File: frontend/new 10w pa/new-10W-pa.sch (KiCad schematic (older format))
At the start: 44 parts, among them K1 D3002, P1 CONN_01X02, P2 CONN_02X01, P3 From HL CN3, P4 CONN_01X02, P5 CONN_01X02, P6 CONN_01X01, P7 From FE CN2, Q1 2N3906, Q2 2N3906, Q3 RD16HHF1, T1 TRANSFO, T2 TRANSFO, U1 74HC14, U2 74HC14

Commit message: Minor updates to v1.12
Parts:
- removed R9: Microstrip, Resistors_SMD:R_0805, symbol R
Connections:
- wire segments 75 -> 79
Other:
- note added: "Microstrip\nW=15Mil, L=1800Mil"
- note added: "T37-6 8T #26"
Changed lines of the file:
@@
 encoding utf-8
 Sheet 1 3
-Title "Hermes-Lite Basic 10W Power Amplifier with Filters"
-Date "Thursday, January 01, 2015"
-Rev "1.11"
+Title "Hermes-Lite Basic 5W Power Amplifier with Filters"
+Date "Friday, January 02, 2015"
+Rev "1.12"
 Comp "SofterHardware"
 Comment1 "AC9HY"
@@
 Connection ~ 8050 3850
 Connection ~ 5650 4200
-$Comp
-L R R9
-U 1 1 54A5A54D
-P 7200 4450
-F 0 "R9" V 7280 4450 40  0000 C CNN
-F 1 "Microstrip" V 7207 4451 40  0000 C CNN
-F 2 "Resistors_SMD:R_0805" V 7130 4450 30  0001 C CNN
-F 3 "" H 7200 4450 30  0000 C CNN
-	1    7200 4450
-	0    1    1    0
-$EndComp
 Wire Wire Line
 	8050 4250 8050 4600
@@
 Wire Wire Line
 	8850 4250 9100 4250
+Text Notes 9350 4050 0    50   ~ 0
+T37-6 8T #26
+Wire Wire Line
+	6950 4450 6950 5000
+Wire Wire Line
+	6950 5000 7150 5000
+Wire Wire Line
+	7150 5000 7150 4450
+Wire Wire Line
+	7150 4450 7450 4450
+Text Notes 6550 5100 0    50   ~ 0
+Microstrip\nW=15Mil, L=1800Mil
 $EndSCHEMATC

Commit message: Starting Layout
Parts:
- R2, R3, R4: footprint Resistors_SMD:R_0805 -> Resistors_ThroughHole:Resistor_Vertical_RM5mm
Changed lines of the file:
@@
 F 0 "R3" V 5180 4050 40  0000 C CNN
 F 1 "0" V 5107 4051 40  0000 C CNN
-F 2 "Resistors_SMD:R_0805" V 5030 4050 30  0001 C CNN
+F 2 "Resistors_ThroughHole:Resistor_Vertical_RM5mm" V 5030 4050 30  0001 C CNN
 F 3 "" H 5100 4050 30  0000 C CNN
 	1    5100 4050
@@
 F 0 "R2" V 4930 4300 40  0000 C CNN
 F 1 "DNI" V 4857 4301 40  0000 C CNN
-F 2 "Resistors_SMD:R_0805" V 4780 4300 30  0001 C CNN
+F 2 "Resistors_ThroughHole:Resistor_Vertical_RM5mm" V 4780 4300 30  0001 C CNN
 F 3 "" H 4850 4300 30  0000 C CNN
 	1    4850 4300
@@
 F 0 "R4" V 5430 4300 40  0000 C CNN
 F 1 "DNI" V 5357 4301 40  0000 C CNN
-F 2 "Resistors_SMD:R_0805" V 5280 4300 30  0001 C CNN
+F 2 "Resistors_ThroughHole:Resistor_Vertical_RM5mm" V 5280 4300 30  0001 C CNN
 F 3 "" H 5350 4300 30  0000 C CNN
 	1    5350 4300

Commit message: Continuing board routing
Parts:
- removed D1: 1N5231, Diodes_SMD:Diode-SMA_Standard, symbol ZENER
- removed Q2: 2N3906, Transistors_SMD:sot23, symbol PNP
- removed R2, R4: DNI, Resistors_ThroughHole:Resistor_Vertical_RM5mm, symbol R
- removed R3: 0, Resistors_ThroughHole:Resistor_Vertical_RM5mm, symbol R
- removed R8: 220, Resistors_SMD:R_0805, symbol R
- removed T2: TRANSFO, Socket_Strips:Socket_Strip_Straight_2x02, symbol TRANSFO
- added T2: OUT_TRANSF, HERMESLITE:OUT_TRANSF, symbol OUT_TRANSFO
- added U7: LP2951-50D, Housings_SOIC:SOIC-8_3.9x4.9mm_Pitch1.27mm, symbol LP2951-50D
- C1, C11, C12, C13, C14, C3, C4, C5, C6, C7, C8, C9: footprint Capacitors_SMD:C_0805 -> HERMESLITE:C_0805
- K1: footprint Sockets_DIP:DIP-10__300 -> HERMESLITE:D3002
- R1, R10, R5, R6: footprint Resistors_SMD:R_0805 -> HERMESLITE:R_0805
- R7: value 1k -> 10k; footprint Resistors_SMD:R_0805 -> HERMESLITE:R_0805
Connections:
- net labels removed: +PTT
- wire segments 79 -> 93
- no-connect marks 13 -> 14
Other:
- moved on the sheet: C5, P6, R7

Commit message: new superband design and updated pcb
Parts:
- C10: footprint Discret:C1V8 -> Capacitors_Tantalum_SMD:TantalC_SizeB_EIA-3528_Reflow
- C2: footprint Discret:C1V8 -> Capacitors_Tantalum_SMD:TantalC_SizeD_EIA-7343_Reflow
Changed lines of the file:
@@
 F 0 "C2" H 5300 1700 50  0000 L CNN
 F 1 "47uF 16V" H 5400 1600 50  0000 L CNN
-F 2 "Discret:C1V8" H 5250 1600 60  0001 C CNN
+F 2 "Capacitors_Tantalum_SMD:TantalC_SizeD_EIA-7343_Reflow" H 5250 1600 60  0001 C CNN
 F 3 "" H 5250 1600 60  0000 C CNN
 	1    5250 1600
@@
 F 0 "C10" H 8300 3100 50  0000 L CNN
 F 1 "10uF 16V" V 8350 2500 50  0000 L CNN
-F 2 "Discret:C1V8" H 8250 3000 60  0001 C CNN
+F 2 "Capacitors_Tantalum_SMD:TantalC_SizeB_EIA-3528_Reflow" H 8250 3000 60  0001 C CNN
 F 3 "" H 8250 3000 60  0000 C CNN
 	1    8250 3000

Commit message: More pcb changes
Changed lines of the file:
@@
 	3400 1800 3400 1700
 Wire Wire Line
-	3400 1700 4700 1700
+	2500 1700 4700 1700
 Wire Wire Line
 	4700 1000 4700 3400
@@
 Connection ~ 8850 4250
 Connection ~ 8850 3850
+Wire Wire Line
+	3400 2000 3400 2050
+Wire Wire Line
+	2500 2050 4900 2050
+Wire Wire Line
+	4900 2050 4900 2150
+$Comp
+L GND #PWR023
+U 1 1 54BBCE74
+P 4900 2150
+F 0 "#PWR023" H 4900 2150 30  0001 C CNN
+F 1 "GND" H 4900 2080 30  0001 C CNN
+F 2 "" H 4900 2150 60  0000 C CNN
+F 3 "" H 4900 2150 60  0000 C CNN
+	1    4900 2150
+	1    0    0    -1
+$EndComp
+Connection ~ 4900 2150
+Wire Wire Line
+	2500 2000 2500 2050
+Connection ~ 3400 2050
+Wire Wire Line
+	2500 1800 2500 1700
+Connection ~ 3400 1700
+Connection ~ 6000 2100
+Connection ~ 5700 2100
+Connection ~ 4400 800
 $EndSCHEMATC

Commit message: BCD Filter update
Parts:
- removed P3: From HL CN3, Pin_Headers:Pin_Header_Straight_2x06, symbol CONN_02X06
- removed P6: CONN_01X01, Pin_Headers:Pin_Header_Straight_1x01, symbol CONN_01X01
- removed P7: From FE CN2, Pin_Headers:Pin_Header_Straight_1x04, symbol CONN_01X04
- removed U1, U2: 74HC14, SMD_Packages:TSSOP-14, symbol 74HC14
- added CN1: BREAKOUT, Pin_Headers:Pin_Header_Straight_2x06, symbol BREAKOUT
- added Q2: 2N3904, Transistors_SMD:sot23, symbol NPN
- added R2, R3: 4.99k, HERMESLITE:R_0805, symbol R
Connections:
- net /PTT is gone; now on net #PTT: R7.1, U7.3 (SHTDN)
- net +12V: now also CN1.6 (12V)
- net GND: now also Q2.1 (E)
- net #PTT: now reaches R1.2
- net #PTT: now also CN1.4 (PTT#), R2.2
- new net: Q2.2 (B), R2.1
- new net 5V: CN1.5 (5V), R3.2
- new net A: CN1.3 (USER0)
- new net B: CN1.2 (USER1)
- new net C: CN1.1 (USER2)
- new net PTT: Q2.3 (C), R3.1
- no-connect marks 14 -> 10
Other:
- note removed: "(Analog Not Imp)"

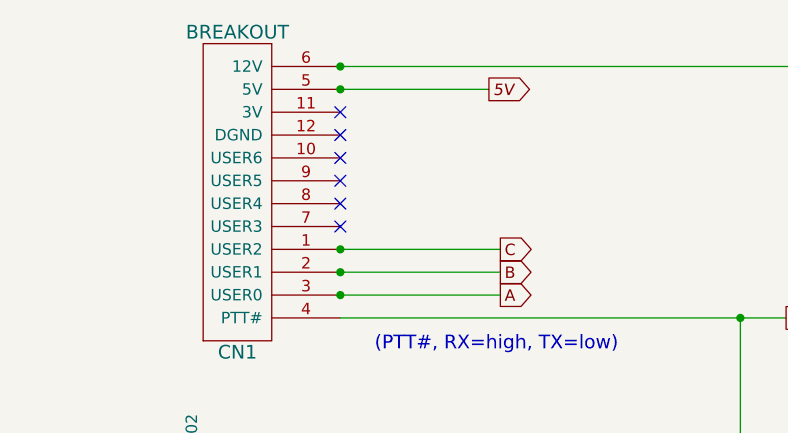
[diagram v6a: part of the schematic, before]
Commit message: Changes for new J16 approach
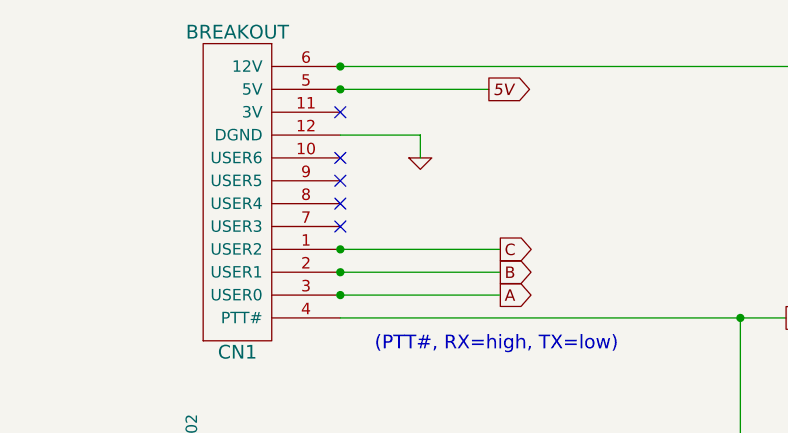
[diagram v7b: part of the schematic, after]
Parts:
- CN1: footprint Pin_Headers:Pin_Header_Straight_2x06 -> HERMESLITE:BREAKOUT
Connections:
- net GND: now also CN1.12 (DGND)
- no-connect marks 10 -> 9
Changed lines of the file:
@@
 F 0 "CN1" H 1300 -50 60  0000 C CNN
 F 1 "BREAKOUT" H 1300 1350 60  0000 C CNN
-F 2 "Pin_Headers:Pin_Header_Straight_2x06" H 1450 600 60  0001 C CNN
+F 2 "HERMESLITE:BREAKOUT" H 1450 600 60  0001 C CNN
 F 3 "" H 1450 600 60  0000 C CNN
 	1    1450 1100
@@
 Wire Wire Line
 	3800 4100 1900 4100
-NoConn ~ 2050 1300
 Wire Wire Line
 	3500 4300 3700 4300
@@
 #PTT
 Connection ~ 3800 2100
+$Comp
+L GND #PWR022
+U 1 1 54C10FCC
+P 2400 1400
+F 0 "#PWR022" H 2400 1400 30  0001 C CNN
+F 1 "GND" H 2400 1330 30  0001 C CNN
+F 2 "" H 2400 1400 60  0000 C CNN
+F 3 "" H 2400 1400 60  0000 C CNN
+	1    2400 1400
+	1    0    0    -1
+$EndComp
+Wire Wire Line
+	2050 1300 2400 1300
+Wire Wire Line
+	2400 1300 2400 1400
 $EndSCHEMATC

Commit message: Final pcd changes
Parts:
- removed Q1: 2N3906, Transistors_SMD:sot23, symbol PNP
- removed Q2: 2N3904, Transistors_SMD:sot23, symbol NPN
- removed R1: 1k, HERMESLITE:R_0805, symbol R
- removed R2, R3: 4.99k, HERMESLITE:R_0805, symbol R
- removed R7: 10k, HERMESLITE:R_0805, symbol R
- added Q1: 2N7000, SMD_Packages:SOT-23-GDS, symbol MOS_N
- added U1: 4050, Housings_SOIC:SOIC-16_3.9x9.9mm_Pitch1.27mm, symbol 4050
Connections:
- net +12V: now also K1.1 (+)
- net A: now also U1.10; no longer CN1.3 (USER0)
- net B: now also U1.6; no longer CN1.2 (USER1)
- net C: now also U1.4; no longer CN1.1 (USER2)
- net GND: now also Q1.S, U1.8 (VSS), U1.8 (VSS), U1.8 (VSS), U1.8 (VSS), U1.8 (VSS); no longer K1.10 (-)
- net at U7.1 (OUT), U7.2 (SNSE): now also K1.8 (C2), Q1.G; no longer VR1.1
- net at K1.7 (T2): now also VR1.1
- net at CN1.7 (USER3): now also U1.3
- net #PTT: no longer names the net of U7.3 (SHTDN)
- net #PTT: now also U1.12; no longer CN1.4 (PTT#)
- net 5V renamed VCC
- net VCC: now also U1.1 (VCC), U1.1 (VCC), U1.1 (VCC), U1.1 (VCC), U1.1 (VCC)
- new net: K1.10 (-), Q1.D
- new net: CN1.1 (USER2), U1.5
- new net: CN1.2 (USER1), U1.7
- new net: CN1.3 (USER0), U1.9
- new net: CN1.4 (PTT#), U1.11
- new net D: U1.2
- no-connect marks 9 -> 6
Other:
- note added: "Note: Using the regulator bias to invert PTT\nto drive the relay. Also sending the bias thru\nthe relay so that the mechanical action is \nsettled prior to applying the bias to the amplifier."
- note removed: "(PTT#, RX=high, TX=low)"
- moved on the sheet: P4, P5
